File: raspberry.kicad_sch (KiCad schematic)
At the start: 3 parts

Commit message: Changes in BOM. Add JLCpcb Part Nr
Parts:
- R410, R411: footprint (none) -> Resistor_SMD:R_0805_2012Metric_Pad1.20x1.40mm_HandSolder; JLCBasicPart (none) -> Basic; JLCPartNr (none) -> C17673; JLCType (none) -> 0805W8F4701T5E; OriginalType (none) -> RK73B2ATTD472J
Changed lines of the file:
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@@
   (symbol (lib_id "power:+5V") (at 151.13 49.53 0) (unit 1)
     (in_bom yes) (on_board yes)
-    (property "Reference" "#PWR?" (id 0) (at 151.13 53.34 0)
+    (property "Reference" "#PWR0101" (id 0) (at 151.13 53.34 0)
       (effects (font (size 1.27 1.27)) hide)
     )
@@
   (symbol (lib_id "power:VCC") (at 158.75 49.53 0) (unit 1)
     (in_bom yes) (on_board yes)
-    (property "Reference" "#PWR?" (id 0) (at 158.75 53.34 0)
+    (property "Reference" "#PWR0102" (id 0) (at 158.75 53.34 0)
       (effects (font (size 1.27 1.27)) hide)
     )
@@
   (symbol (lib_id "power:VCC") (at 203.2 49.53 0) (unit 1)
     (in_bom yes) (on_board yes)
-    (property "Reference" "#PWR?" (id 0) (at 203.2 53.34 0)
+    (property "Reference" "#PWR0104" (id 0) (at 203.2 53.34 0)
       (effects (font (size 1.27 1.27)) hide)
     )
@@
   (symbol (lib_id "power:GND") (at 153.67 129.54 0) (unit 1)
     (in_bom yes) (on_board yes)
-    (property "Reference" "#PWR?" (id 0) (at 153.67 135.89 0)
+    (property "Reference" "#PWR0103" (id 0) (at 153.67 135.89 0)
       (effects (font (size 1.27 1.27)) hide)
     )
@@
       (effects (font (size 1.27 1.27)) (justify left))
     )
-    (property "Footprint" "" (id 2) (at 196.342 68.58 90)
+    (property "Footprint" "Resistor_SMD:R_0805_2012Metric_Pad1.20x1.40mm_HandSolder" (id 2) (at 196.342 68.58 90)
       (effects (font (size 1.27 1.27)) hide)
     )
     (property "Datasheet" "~" (id 3) (at 198.12 68.58 0)
+      (effects (font (size 1.27 1.27)) hide)
+    )
+    (property "JLCBasicPart" "Basic" (id 4) (at 198.12 68.58 0)
+      (effects (font (size 1.27 1.27)) hide)
+    )
+    (property "JLCPartNr" "C17673" (id 5) (at 198.12 68.58 0)
+      (effects (font (size 1.27 1.27)) hide)
+    )
+    (property "JLCType" "0805W8F4701T5E" (id 6) (at 198.12 68.58 0)
+      (effects (font (size 1.27 1.27)) hide)
+    )
+    (property "OriginalType" "RK73B2ATTD472J" (id 7) (at 198.12 68.58 0)
       (effects (font (size 1.27 1.27)) hide)
     )
@@
       (effects (font (size 1.27 1.27)) (justify left))
     )
-    (property "Footprint" "" (id 2) (at 206.502 68.58 90)
+    (property "Footprint" "Resistor_SMD:R_0805_2012Metric_Pad1.20x1.40mm_HandSolder" (id 2) (at 206.502 68.58 90)
       (effects (font (size 1.27 1.27)) hide)
     )
@@
       (effects (font (size 1.27 1.27)) hide)
     )
+    (property "JLCBasicPart" "Basic" (id 4) (at 208.28 68.58 0)
+      (effects (font (size 1.27 1.27)) hide)
+    )
+    (property "JLCPartNr" "C17673" (id 5) (at 208.28 68.58 0)
+      (effects (font (size 1.27 1.27)) hide)
+    )
+    (property "JLCType" "0805W8F4701T5E" (id 6) (at 208.28 68.58 0)
+      (effects (font (size 1.27 1.27)) hide)
+    )
+    (property "OriginalType" "RK73B2ATTD472J" (id 7) (at 208.28 68.58 0)
+      (effects (font (size 1.27 1.27)) hide)
+    )

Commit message: working on BOM. Small Fixes in Schematics
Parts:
- JP400: footprint (none) -> Connector_PinHeader_2.54mm:PinHeader_2x20_P2.54mm_Vertical; JLCBasicPart (none) -> Extended; JLCPartNr (none) -> C35165; OriginalType (none) -> C35165; Supplier (none) -> LCSC
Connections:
- net EXT_TRIGGER: no longer names the net of JP400.36 (GPIO16)
- no-connect marks 12 -> 13
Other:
- note added: "EXT_TRIGGER"
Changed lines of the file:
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@@
   (junction (at 203.2 59.69) (diameter 1.016) (color 0 0 0 0))
   (junction (at 208.28 78.74) (diameter 1.016) (color 0 0 0 0))
+  (no_connect (at 134.62 76.2))
   (no_connect (at 134.62 78.74))
   (no_connect (at 134.62 86.36))
@@
     (stroke (width 0) (type solid) (color 0 0 0 0))
   )
-  (wire (pts (xy 125.73 76.2) (xy 134.62 76.2))
-    (stroke (width 0) (type solid) (color 0 0 0 0))
-  )
   (wire (pts (xy 125.73 81.28) (xy 134.62 81.28))
     (stroke (width 0) (type solid) (color 0 0 0 0))
@@
   (wire (pts (xy 208.28 78.74) (xy 209.55 78.74))
     (stroke (width 0) (type solid) (color 0 0 0 0))
+  )
+  (text "EXT_TRIGGER" (at 113.03 77.47 0)
+    (effects (font (size 1.27 1.27)) (justify left bottom))
   )
   (text "PREAMP2_EN" (at 125.73 80.01 180)
@@
     )
   )
-  (global_label "EXT_TRIGGER" (shape input) (at 125.73 76.2 180)
-    (effects (font (size 1.27 1.27)) (justify right))
-    (property "Intersheet References" "${INTERSHEET_REFS}" (id 0) (at 109.6977 76.1206 0)
-      (effects (font (size 1.27 1.27)) (justify right) hide)
-    )
-  )
   (global_label "TIMEPULSE" (shape input) (at 125.73 81.28 180)
     (effects (font (size 1.27 1.27)) (justify right))
@@
     (property "Reference" "JP400" (id 0) (at 165.1 56.4896 0))
     (property "Value" "Raspberry_Pi_2_3" (id 1) (at 170.18 58.7945 0))
-    (property "Footprint" "" (id 2) (at 154.94 91.44 0)
+    (property "Footprint" "Connector_PinHeader_2.54mm:PinHeader_2x20_P2.54mm_Vertical" (id 2) (at 154.94 91.44 0)
       (effects (font (size 1.27 1.27)) hide)
     )
@@
       (effects (font (size 1.27 1.27)) hide)
     )
+    (property "JLCBasicPart" "Extended" (id 4) (at 154.94 91.44 0)
+      (effects (font (size 1.27 1.27)) hide)
+    )
+    (property "JLCPartNr" "C35165" (id 5) (at 154.94 91.44 0)
+      (effects (font (size 1.27 1.27)) hide)
+    )
+    (property "OriginalType" "C35165 " (id 6) (at 154.94 91.44 0)
+      (effects (font (size 1.27 1.27)) hide)
+    )
+    (property "Supplier" "LCSC" (id 7) (at 154.94 91.44 0)
+      (effects (font (size 1.27 1.27)) hide)
+    )

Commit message: Started PCB. Placed Parts
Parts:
- JP400: footprint Connector_PinHeader_2.54mm:PinHeader_2x20_P2.54mm_Vertical -> Connector_PinSocket_2.54mm:PinSocket_2x20_P2.54mm_Vertical
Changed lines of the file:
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@@
     (property "Reference" "JP400" (id 0) (at 165.1 56.4896 0))
     (property "Value" "Raspberry_Pi_2_3" (id 1) (at 170.18 58.7945 0))
-    (property "Footprint" "Connector_PinHeader_2.54mm:PinHeader_2x20_P2.54mm_Vertical" (id 2) (at 154.94 91.44 0)
+    (property "Footprint" "Connector_PinSocket_2.54mm:PinSocket_2x20_P2.54mm_Vertical" (id 2) (at 154.94 91.44 0)
       (effects (font (size 1.27 1.27)) hide)
     )

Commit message: Progress in PCB. Some changes in Schematis. Solderjumper for modular design added.
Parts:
- added H1, H2, H3, H4: MountingHole, MountingHole:MountingHole_2.7mm_M2.5, symbol Mechanical:MountingHole
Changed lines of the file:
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@@
     (pin "1")
+  )
+  (symbol (lib_id "Mechanical:MountingHole") (at 86.36 172.72 0) (unit 1)
+    (in_bom no) (on_board yes) (fields_autoplaced)
+    (property "Reference" "H1" (id 0) (at 88.9001 171.9591 0)
+      (effects (font (size 1.27 1.27)) (justify left))
+    )
+    (property "Value" "MountingHole" (id 1) (at 88.9001 174.2578 0)
+      (effects (font (size 1.27 1.27)) (justify left))
+    )
+    (property "Footprint" "MountingHole:MountingHole_2.7mm_M2.5" (id 2) (at 86.36 172.72 0)
+      (effects (font (size 1.27 1.27)) hide)
+    )
+    (property "Datasheet" "~" (id 3) (at 86.36 172.72 0)
+      (effects (font (size 1.27 1.27)) hide)
+    )
+  )
+  (symbol (lib_id "Mechanical:MountingHole") (at 86.36 177.8 0) (unit 1)
+    (in_bom no) (on_board yes) (fields_autoplaced)
+    (property "Reference" "H2" (id 0) (at 88.9001 177.0391 0)
+      (effects (font (size 1.27 1.27)) (justify left))
+    )
+    (property "Value" "MountingHole" (id 1) (at 88.9001 179.3378 0)
+      (effects (font (size 1.27 1.27)) (justify left))
+    )
+    (property "Footprint" "MountingHole:MountingHole_2.7mm_M2.5" (id 2) (at 86.36 177.8 0)
+      (effects (font (size 1.27 1.27)) hide)
+    )
+    (property "Datasheet" "~" (id 3) (at 86.36 177.8 0)
+      (effects (font (size 1.27 1.27)) hide)
+    )
+  )
+  (symbol (lib_id "Mechanical:MountingHole") (at 86.36 182.88 0) (unit 1)
+    (in_bom no) (on_board yes) (fields_autoplaced)
+    (property "Reference" "H3" (id 0) (at 88.9001 182.1191 0)
+      (effects (font (size 1.27 1.27)) (justify left))
+    )
+    (property "Value" "MountingHole" (id 1) (at 88.9001 184.4178 0)
+      (effects (font (size 1.27 1.27)) (justify left))
+    )
+    (property "Footprint" "MountingHole:MountingHole_2.7mm_M2.5" (id 2) (at 86.36 182.88 0)
+      (effects (font (size 1.27 1.27)) hide)
+    )
+    (property "Datasheet" "~" (id 3) (at 86.36 182.88 0)
+      (effects (font (size 1.27 1.27)) hide)
+    )
+  )
+  (symbol (lib_id "Mechanical:MountingHole") (at 86.36 187.96 0) (unit 1)
+    (in_bom no) (on_board yes) (fields_autoplaced)
+    (property "Reference" "H4" (id 0) (at 88.9001 187.1991 0)
+      (effects (font (size 1.27 1.27)) (justify left))
+    )
+    (property "Value" "MountingHole" (id 1) (at 88.9001 189.4978 0)
+      (effects (font (size 1.27 1.27)) (justify left))
+    )
+    (property "Footprint" "MountingHole:MountingHole_2.7mm_M2.5" (id 2) (at 86.36 187.96 0)
+      (effects (font (size 1.27 1.27)) hide)
+    )
+    (property "Datasheet" "~" (id 3) (at 86.36 187.96 0)
+      (effects (font (size 1.27 1.27)) hide)
+    )
   )
   (symbol (lib_id "Device:R") (at 198.12 68.58 0) (unit 1)

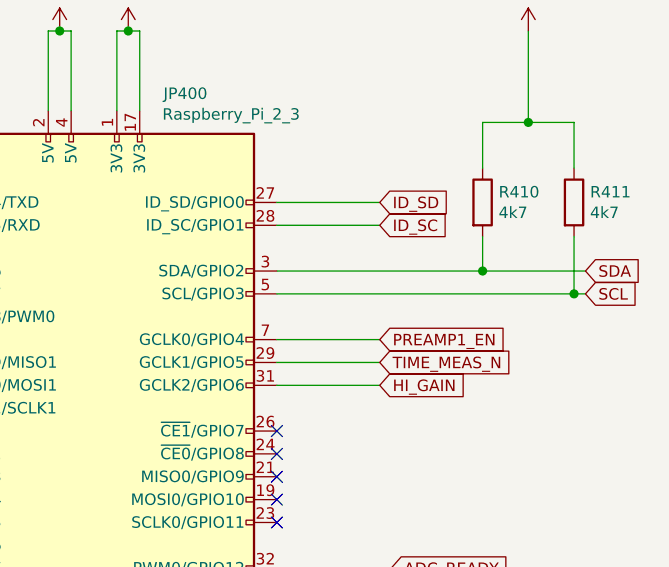
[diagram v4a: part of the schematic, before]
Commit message: Silkscreen edided. Minor improvements
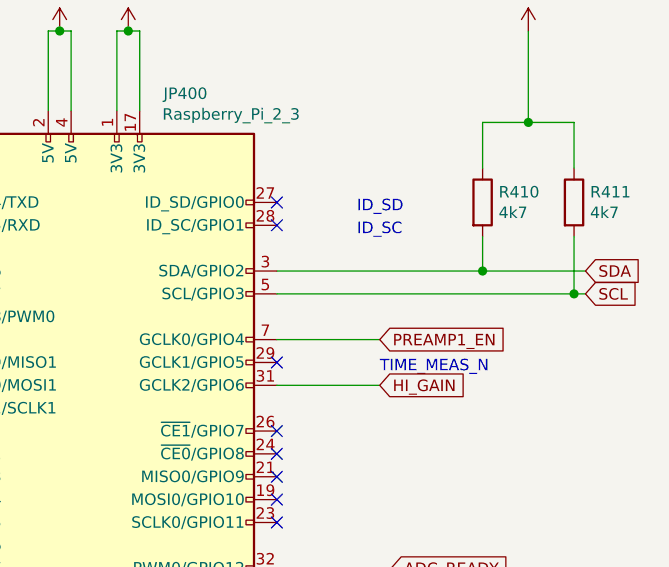
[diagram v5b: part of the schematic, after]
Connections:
- net ID_SC: no longer names the net of JP400.28 (ID_SC/GPIO1)
- net ID_SD: no longer names the net of JP400.27 (ID_SD/GPIO0)
- net TIME_MEAS_N: no longer names the net of JP400.29 (GCLK1/GPIO5)
- no-connect marks 13 -> 16
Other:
- note added: "ID_SC"
- note added: "ID_SD"
- note added: "TIME_MEAS_N"
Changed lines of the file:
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@@
   (no_connect (at 134.62 101.6))
   (no_connect (at 134.62 104.14))
+  (no_connect (at 175.26 68.58))
+  (no_connect (at 175.26 71.12))
+  (no_connect (at 175.26 86.36))
   (no_connect (at 175.26 93.98))
   (no_connect (at 175.26 96.52))
@@
     (stroke (width 0) (type solid) (color 0 0 0 0))
   )
-  (wire (pts (xy 175.26 68.58) (xy 186.69 68.58))
-    (stroke (width 0) (type solid) (color 0 0 0 0))
-  )
-  (wire (pts (xy 175.26 71.12) (xy 186.69 71.12))
-    (stroke (width 0) (type solid) (color 0 0 0 0))
-  )
   (wire (pts (xy 175.26 76.2) (xy 198.12 76.2))
     (stroke (width 0) (type solid) (color 0 0 0 0))
@@
     (stroke (width 0) (type solid) (color 0 0 0 0))
   )
-  (wire (pts (xy 175.26 86.36) (xy 186.69 86.36))
-    (stroke (width 0) (type solid) (color 0 0 0 0))
-  )
   (wire (pts (xy 175.26 88.9) (xy 186.69 88.9))
     (stroke (width 0) (type solid) (color 0 0 0 0))
@@
     (effects (font (size 1.27 1.27)) (justify right bottom))
   )
+  (text "ID_SD" (at 184.15 69.85 0)
+    (effects (font (size 1.27 1.27)) (justify left bottom))
+  )
+  (text "ID_SC" (at 184.15 72.39 0)
+    (effects (font (size 1.27 1.27)) (justify left bottom))
+  )
+  (text "TIME_MEAS_N" (at 186.69 87.63 0)
+    (effects (font (size 1.27 1.27)) (justify left bottom))
+  )
   (global_label "GPS_RXD" (shape input) (at 125.73 68.58 180)
     (effects (font (size 1.27 1.27)) (justify right))
@@
     (property "Intersheet References" "${INTERSHEET_REFS}" (id 0) (at 113.81 109.1406 0)
       (effects (font (size 1.27 1.27)) (justify right) hide)
-    )
-  )
-  (global_label "ID_SD" (shape input) (at 186.69 68.58 0)
-    (effects (font (size 1.27 1.27)) (justify left))
-    (property "Intersheet References" "${INTERSHEET_REFS}" (id 0) (at 195.949 68.5006 0)
-      (effects (font (size 1.27 1.27)) (justify left) hide)
-    )
-  )
-  (global_label "ID_SC" (shape input) (at 186.69 71.12 0)
-    (effects (font (size 1.27 1.27)) (justify left))
-    (property "Intersheet References" "${INTERSHEET_REFS}" (id 0) (at 195.949 71.0406 0)
-      (effects (font (size 1.27 1.27)) (justify left) hide)
     )
   )
@@
       (effects (font (size 1.27 1.27)) (justify left) hide)
     )
-  )
-  (global_label "TIME_MEAS_N" (shape input) (at 186.69 86.36 0)
-    (effects (font (size 1.27 1.27)) (justify left))
-    (property "Intersheet References" "${INTERSHEET_REFS}" (id 0) (at 202.9642 86.4394 0)
-      (effects (font (size 1.27 1.27)) (justify left) hide)
-    )

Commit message: Redesign of Board. Added optional Breakoutboars for ADC and DAC
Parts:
- JP400: footprint Connector_PinSocket_2.54mm:PinSocket_2x20_P2.54mm_Vertical -> Connector_IDC:IDC-Header_2x20_P2.54mm_Vertical
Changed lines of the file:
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@@
     (property "Reference" "JP400" (id 0) (at 165.1 56.4896 0))
     (property "Value" "Raspberry_Pi_2_3" (id 1) (at 170.18 58.7945 0))
-    (property "Footprint" "Connector_PinSocket_2.54mm:PinSocket_2x20_P2.54mm_Vertical" (id 2) (at 154.94 91.44 0)
+    (property "Footprint" "Connector_IDC:IDC-Header_2x20_P2.54mm_Vertical" (id 2) (at 154.94 91.44 0)
       (effects (font (size 1.27 1.27)) hide)
     )

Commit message: some changes after first test of boards. Package of SN74LV221AD changed to SOIC-16.
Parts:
- H1, H2, H3, H4: Supplier (none) -> --
- R410, R411: JLCplace (none) -> C17673; Supplier (none) -> LCSC
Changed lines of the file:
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@@
+      (effects (font (size 1.27 1.27)) hide)
+    )
+    (property "Supplier" "--" (id 4) (at 86.36 172.72 0)
       (effects (font (size 1.27 1.27)) hide)
     )
@@
       (effects (font (size 1.27 1.27)) hide)
     )
+    (property "Supplier" "--" (id 4) (at 86.36 177.8 0)
+      (effects (font (size 1.27 1.27)) hide)
+    )
   )
   (symbol (lib_id "Mechanical:MountingHole") (at 86.36 182.88 0) (unit 1)
@@
       (effects (font (size 1.27 1.27)) hide)
     )
+    (property "Supplier" "--" (id 4) (at 86.36 182.88 0)
+      (effects (font (size 1.27 1.27)) hide)
+    )
   )
   (symbol (lib_id "Mechanical:MountingHole") (at 86.36 187.96 0) (unit 1)
@@
     )
     (property "Datasheet" "~" (id 3) (at 86.36 187.96 0)
+      (effects (font (size 1.27 1.27)) hide)
+    )
+    (property "Supplier" "--" (id 4) (at 86.36 187.96 0)
       (effects (font (size 1.27 1.27)) hide)
     )
@@
     )
     (property "OriginalType" "RK73B2ATTD472J" (id 7) (at 198.12 68.58 0)
+      (effects (font (size 1.27 1.27)) hide)
+    )
+    (property "Supplier" "LCSC" (id 8) (at 198.12 68.58 0)
+      (effects (font (size 1.27 1.27)) hide)
+    )
+    (property "JLCplace" "C17673" (id 9) (at 198.12 68.58 0)
       (effects (font (size 1.27 1.27)) hide)
     )
@@
       (effects (font (size 1.27 1.27)) hide)
     )
+    (property "Supplier" "LCSC" (id 8) (at 208.28 68.58 0)
+      (effects (font (size 1.27 1.27)) hide)
+    )
+    (property "JLCplace" "C17673" (id 9) (at 208.28 68.58 0)
+      (effects (font (size 1.27 1.27)) hide)
+    )
